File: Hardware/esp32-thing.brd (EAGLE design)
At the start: 25.4 x 58.9 mm, 71 parts, among them Q1 2.5A/30V, Q2 MBT3904DW1T1, U1 MCP73831, U3 AP2112K-3.3V, U4 FT231XS, U5 W25Q32FVSS, Y1 26MHz, Y2 32.768kHz

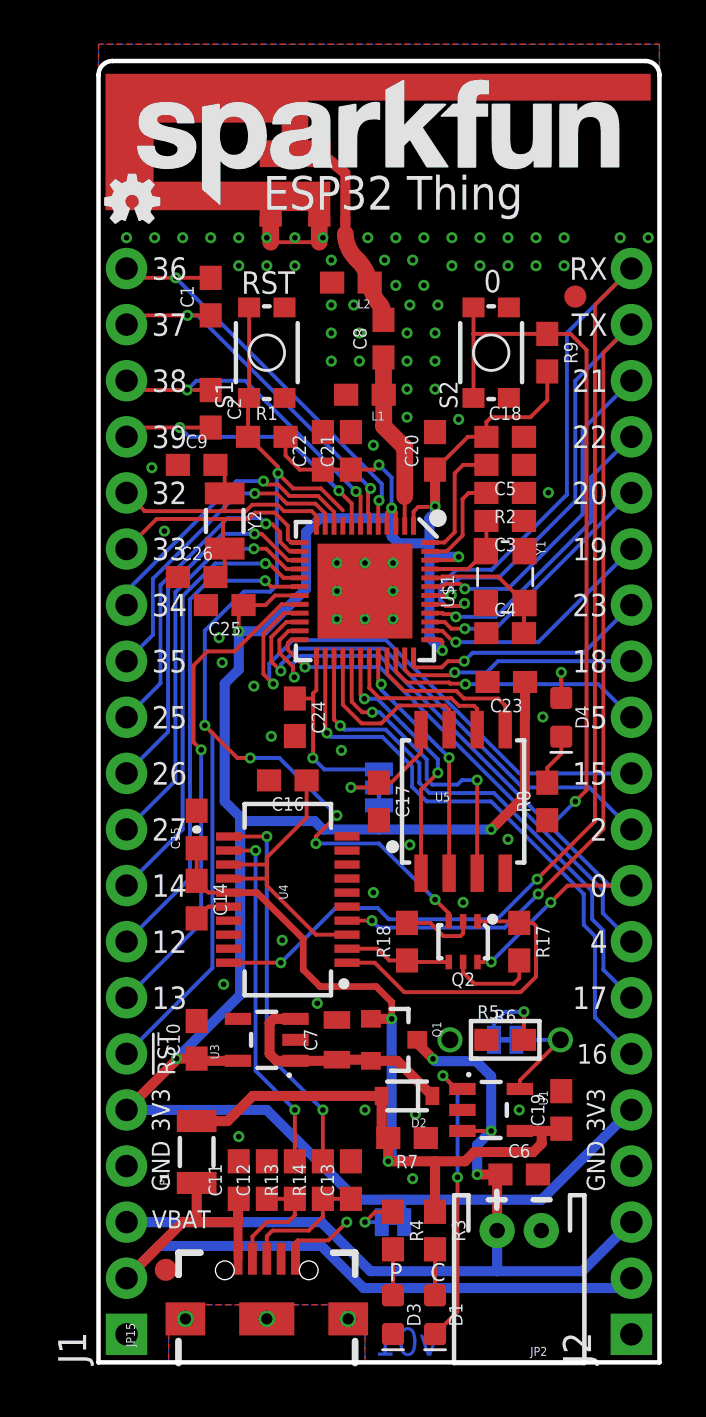
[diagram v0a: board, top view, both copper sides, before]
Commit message: Fixing reset pin wiring.
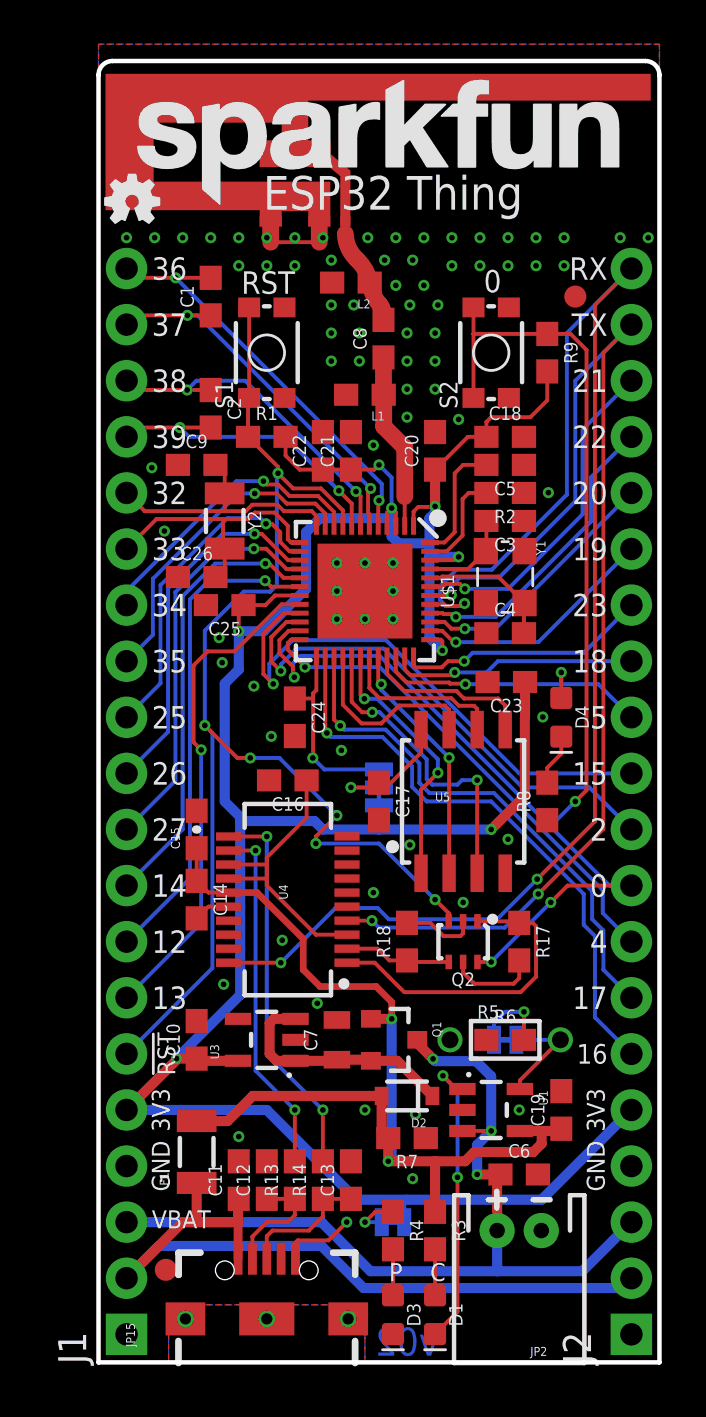
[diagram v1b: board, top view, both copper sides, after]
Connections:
- net CHIP_PU: now also U$1.9
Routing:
- net CHIP_PU: track 58.9 -> 59.6 mm
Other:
- board text added: "v02"
- board text removed: "v01"
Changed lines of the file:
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@@
 <layer number="47" name="Measures" color="7" fill="1" visible="no" active="yes"/>
 <layer number="48" name="Document" color="7" fill="1" visible="no" active="yes"/>
-<layer number="49" name="Reference" color="7" fill="1" visible="yes" active="yes"/>
+<layer number="49" name="Reference" color="7" fill="1" visible="no" active="yes"/>
 <layer number="50" name="dxf" color="7" fill="1" visible="no" active="no"/>
 <layer number="51" name="tDocu" color="6" fill="1" visible="yes" active="yes"/>
@@
 <text x="18.288" y="13.335" size="0.8128" layer="22" font="vector" ratio="15" rot="MR0" align="top-center">SJ1</text>
 <text x="13.843" y="26.162" size="0.8128" layer="22" font="vector" ratio="15" rot="MR270" align="top-center">SJ3</text>
-<text x="13.97" y="0.3048" size="1.27" layer="16" font="vector" ratio="15" rot="MR0" align="bottom-center">v01</text>
+<text x="13.97" y="0.3048" size="1.27" layer="16" font="vector" ratio="15" rot="MR0" align="bottom-center">v02</text>
 <text x="13.97" y="-19.05" size="1.778" layer="51" font="vector" ratio="15">Jim Lindblom</text>
 <text x="13.462" y="3.683" size="0.8128" layer="21" font="vector" ratio="15" align="bottom-center">P</text>
@@
 <wire x1="15.86" y1="19.97" x2="15.86" y2="20.335" width="0.1778" layer="1"/>
 <wire x1="15.86" y1="20.335" x2="15.24" y2="20.955" width="0.1778" layer="1"/>
+<contactref element="U$1" pad="9"/>
+<wire x1="11.065" y1="38.5793" x2="11.065" y2="37.875" width="0.1778" layer="1"/>
 </signal>
 <signal name="GND">

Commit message: Fixing ESP32 pin map, re-routing RX, TX
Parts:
- added C27: 3.3nF, SparkFun-Capacitors:0603
- U$2: value ESP32 -> ESP32-2
- moved C5 2.54 mm to (21.0, 40.6), turned to 90 degrees
- moved C18 2.01 mm to (16.5, 41.3), turned to 90 degrees
- moved R2 1.27 mm to (18.4, 40.6), turned to 90 degrees
- renumbered U$1 to U$2
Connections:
- removed net 20: J2.16, U$2.39
- removed net RES_14K: R2.2, U$2.47
- new net N$4: C27.2, R2.1, U$2.47
- net 16: now also U$2.25; no longer U$2.26
- net 21: now also J2.19, U$2.42; no longer J2.18, U$2.43
- net 22: now also J2.16, U$2.39; no longer J2.17, U$2.40
- net 3.3V: now also U$2.43
- net CAP_10N: now also C27.1, R2.2
- net FLASH_VDD: now also U$2.26; no longer U$2.25
- net GND: now also J2.20; no longer R2.1
- net U0RXD: now also J2.17, U$2.40; no longer J2.20, U$2.41
- net U0TXD: now also J2.18, U$2.41; no longer J2.19, U$2.42
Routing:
- net U0RXD: track 67.9 -> 53.2 mm
- net 20: track 11.8 -> 0.00 mm, vias 1 -> 0
- net N$4: track 0.00 -> 6.55 mm
- net RES_14K: track 4.61 -> 0.00 mm
- net 21: track 15.4 -> 19.0 mm
- net U0TXD: track 54.6 -> 51.3 mm
- net CAP_10N: track 5.57 -> 8.72 mm
- net 3.3V: track 123.7 -> 126.6 mm, vias 8 -> 9
- net 37: track 17.3 -> 19.9 mm, vias 2 -> 1
- net 38: track 15.5 -> 18.1 mm, vias 2 -> 1
- net 36: track 19.2 -> 21.5 mm, vias 2 -> 1
- net 39: track 14.2 -> 16.4 mm, vias 2 -> 1
- net GND: track 9.19 -> 10.3 mm, vias 78 -> 79
- net 22: track 13.7 -> 13.2 mm
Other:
- board text removed: "20"

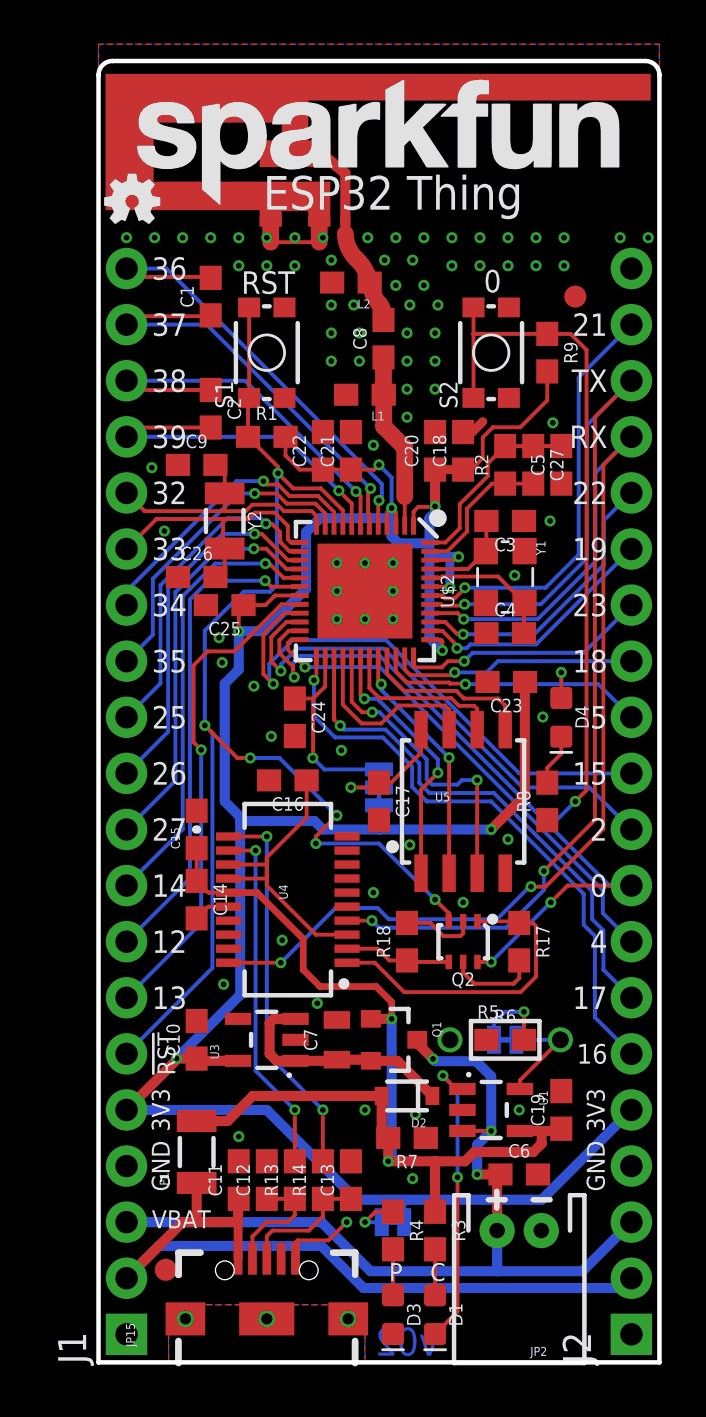
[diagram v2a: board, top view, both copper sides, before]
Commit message: Re-routing i/o traces to get better ground fill.
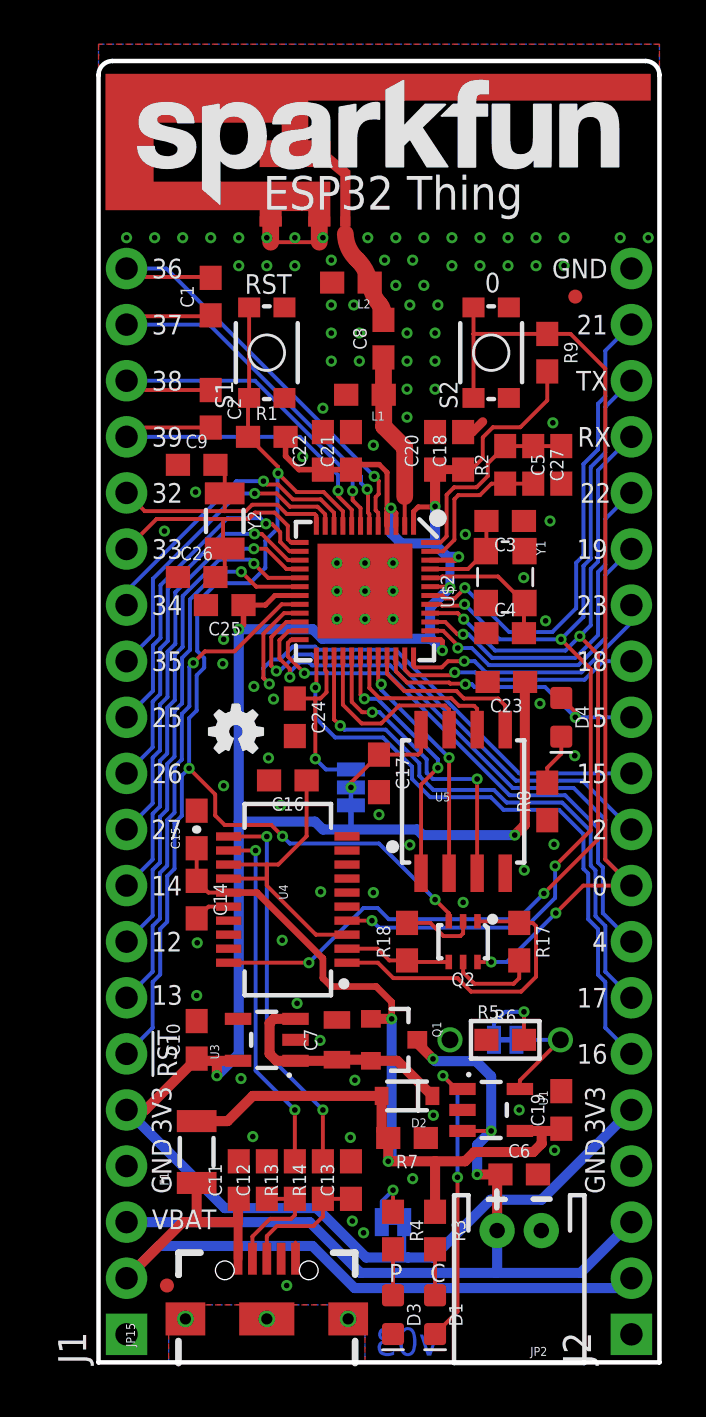
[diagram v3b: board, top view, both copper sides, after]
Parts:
- C27: value 3.3nF -> 3.0nF; device SparkFun-Capacitors:0603 -> esp32-thing-temp:0603
- FD1, FD2: value FIDUCIAL1X2 -> FIDUCIALUFIDUCIAL; device SparkFun-Aesthetics:FIDUCIAL-1X2 -> SparkFun-Aesthetics:MICRO-FIDUCIAL
- LOGO3: value SFE_LOGO_NAME.1_INCH -> SFE_LOGO_NAME.2_INCH; device SparkFun-Aesthetics:SFE_LOGO_NAME_.1 -> SparkFun-Aesthetics:SFE_LOGO_NAME_.2
- R2: value 14k -> 20k; device esp32-thing-temp:0603 -> SparkFun-Resistors:0603
- moved LOGO2 24.5 mm to (6.22, 28.6)
- moved LOGO3 3.33 mm to (23.7, 53.2)
- moved C17 1.27 mm to (12.7, 26.7)
- moved SJ3 1.27 mm to (11.4, 26.0)
- moved FD1 0.71 mm to (3.10, 3.48)
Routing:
- net U0TXD: track 51.3 -> 42.7 mm, vias 3 -> 4
- net U0RXD: track 53.2 -> 47.0 mm, vias 3 -> 4
- net 0: track 63.6 -> 67.1 mm, vias 4 -> 3
- net 21: track 19.0 -> 22.0 mm
- net GND: track 10.3 -> 7.57 mm, vias 79 -> 97
- net 22: track 13.2 -> 15.8 mm
- net 19: track 11.4 -> 13.7 mm
- net 3.3V: track 126.6 -> 128.7 mm, vias 9 -> 8
- net 4: track 22.6 -> 24.3 mm
- net CHIP_PU: track 59.6 -> 58.1 mm, vias 6 -> 4
- net 17: track 23.9 -> 25.2 mm
- net 16: track 27.0 -> 28.3 mm
- net N$11: track 6.15 -> 4.97 mm
- net FLASH_VDD: track 8.88 -> 7.75 mm
- net 23: track 11.5 -> 12.4 mm
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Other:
- board text added: "CHG PROG"
- board text added: "PWR-LED EN"
- board text added: "v03"
- board text removed: "SJ1"
- board text removed: "SJ2"
- board text removed: "v02"

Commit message: Optimizing some routing.
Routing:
- net 16: track 28.3 -> 27.4 mm
- net 17: track 25.2 -> 24.3 mm
- net 4: track 24.3 -> 23.3 mm
- net 3.3V: track 128.7 -> 128.0 mm
- net 0: track 67.1 -> 67.7 mm
- net U0RXD: track 47.0 -> 47.5 mm
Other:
- board text added: "PWR LED"
- board text removed: "PWR-LED EN"

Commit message: Post-review fixes - changed C18 to 100pF
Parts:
- C18: value 0.1uF -> 100pF
- R1, R9: value 10K -> 10k
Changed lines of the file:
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@@
 <attribute name="PROD_ID" value="SWCH-13065" x="7.62" y="45.72" size="1.778" layer="27" font="vector" ratio="15" rot="R90" display="off"/>
 </element>
-<element name="R1" library="SparkFun-Resistors" package="0603" value="10K" x="7.62" y="41.91">
+<element name="R1" library="SparkFun-Resistors" package="0603" value="10k" x="7.62" y="41.91">
 <attribute name="PROD_ID" value="RES-00824" x="7.62" y="41.91" size="1.778" layer="27" font="vector" ratio="15" display="off"/>
 </element>
@@
 <attribute name="PROD_ID" value="RES-00824" x="7.62" y="7.62" size="1.778" layer="27" font="vector" ratio="15" rot="R90" display="off"/>
 </element>
-<element name="C18" library="SparkFun-Capacitors" package="0603" value="0.1uF" x="16.51" y="41.275" rot="R90">
-<attribute name="PROD_ID" value="CAP-00810" x="16.51" y="41.275" size="1.778" layer="27" font="vector" ratio="15" rot="R90" display="off"/>
+<element name="C18" library="SparkFun-Capacitors" package="0603" value="100pF" x="16.51" y="41.275" rot="R90">
+<attribute name="PROD_ID" value="CAP-07883" x="16.51" y="41.275" size="1.778" layer="27" font="vector" ratio="15" rot="R90" display="off"/>
 </element>
 <element name="C20" library="SparkFun-Capacitors" package="0603" value="0.1uF" x="15.24" y="41.275" rot="R90">
@@
 <element name="FD2" library="SparkFun-Aesthetics" package="MICRO-FIDUCIAL" value="FIDUCIALUFIDUCIAL" x="21.59" y="48.26"/>
 <element name="LOGO3" library="SparkFun-Aesthetics" package="SFE_LOGO_NAME_.2" value="SFE_LOGO_NAME.2_INCH" x="23.749" y="53.213" rot="MR0"/>
-<element name="R9" library="SparkFun-Resistors" package="0603" value="10K" x="20.32" y="45.72" rot="R270">
+<element name="R9" library="SparkFun-Resistors" package="0603" value="10k" x="20.32" y="45.72" rot="R270">
 <attribute name="PROD_ID" value="RES-00824" x="20.32" y="45.72" size="1.778" layer="27" font="vector" ratio="15" rot="R270" display="off"/>
 </element>

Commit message: Post-checklist fixes.
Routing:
- net N$11: track 4.97 -> 6.93 mm
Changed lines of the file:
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@@
 <wire x1="12.7" y1="27.52" x2="14.4771" y2="27.52" width="0.1778" layer="1"/>
 <wire x1="14.4771" y1="27.52" x2="14.605" y2="27.6479" width="0.1778" layer="1"/>
-<via x="11.43" y="26.035" extent="1-16" drill="0.254"/>
-<wire x1="12.7" y1="27.52" x2="11.43" y2="26.25" width="0.1778" layer="1"/>
-<wire x1="11.43" y1="26.25" x2="11.43" y2="26.035" width="0.1778" layer="1"/>
+<via x="10.3886" y="26.035" extent="1-16" drill="0.254"/>
+<wire x1="10.3886" y1="26.035" x2="11.43" y2="26.035" width="0.1778" layer="16"/>
+<wire x1="10.3886" y1="26.035" x2="11.215" y2="26.035" width="0.1778" layer="1"/>
+<wire x1="11.215" y1="26.035" x2="12.7" y2="27.52" width="0.1778" layer="1"/>
 </signal>
 <signal name="FLASH_VDD">

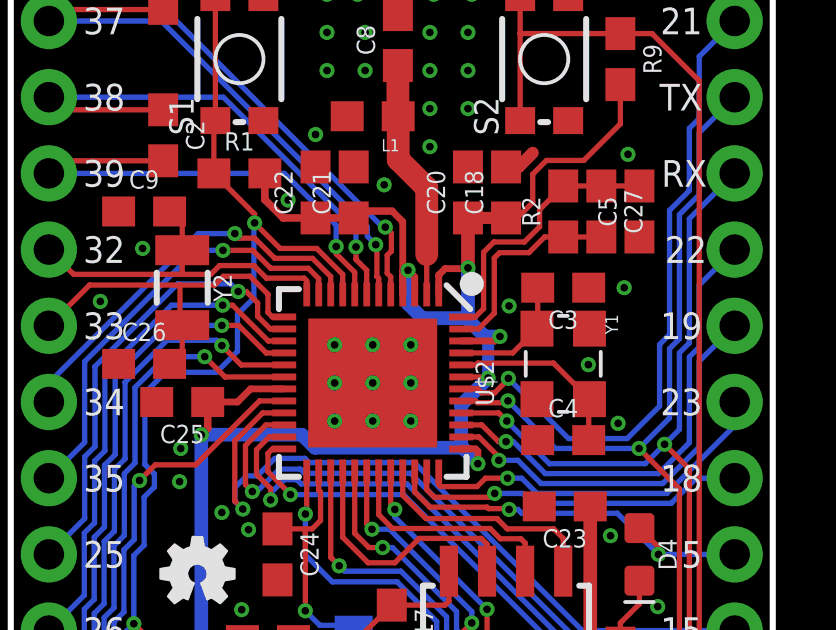
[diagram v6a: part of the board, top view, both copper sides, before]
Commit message: Fixing v03 checklist issues.
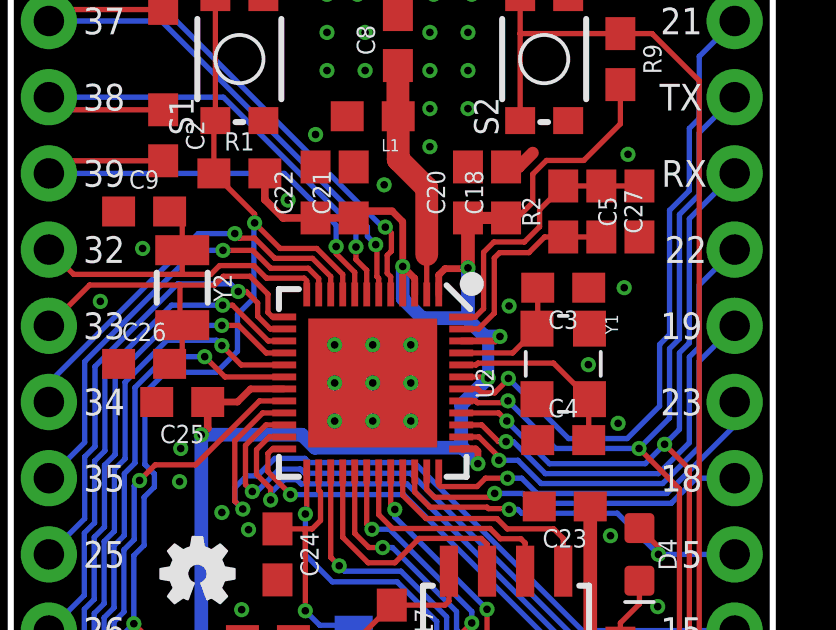
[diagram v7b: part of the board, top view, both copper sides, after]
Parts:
- U2: value ESP32-2 -> ESP3212
- renumbered U$2 to U2
